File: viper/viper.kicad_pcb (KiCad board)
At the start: 2 copper layers, 49 parts, among them J1 Barrel_Jack, J10 DEBUG PINS, J11 Conn_01x05_Male, J12 Pimoroni BLINKT!, J13 Pimoroni BLINKT!, J2 Raspberry Pi Zero W2, J3 RPI Headers, J4 Adafruit CharliePlex Bonnet, J5 RPI Headers, J6 Pimoroni BLINKT!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

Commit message: feat: off switch routing
Signed-off-by: Matt Gleich <git@mattglei.ch>
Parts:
- J10, J7, J8: footprint Connector_PinHeader_2.54mm:PinHeader_2x20_P2.54mm_Vertical -> Connector_PinHeader_2.54mm:PinHeader_2x02_P2.54mm_Vertical
- R1, R10, R11, R12, R2, R3, R4, R5, R6, R7, R8, R9: value R_US -> 330Ω
- S1: value M2012SA1W03 -> MARK I
- S2: value M2012SA1W03 -> MARK II
- S3: value M2012SA1W03 -> MARK III
- S4: value M2012SA1W03 -> MARK IV
- S5: value M2012SA1W03 -> MASTER
- S6: value M2012SA1W03 -> MARK V
- moved D5 181.5 mm to (78.7, 21.3), turned to 180 degrees
- moved S3 179.3 mm to (77.9, 36.2), turned to 180 degrees
- moved D7 176.3 mm to (111.7, 21.5), turned to 180 degrees
- moved S4 167.2 mm to (110.7, 36.2), turned to 180 degrees
- moved D3 165.4 mm to (95.0, 21.4), turned to 180 degrees
- moved D2 160.3 mm to (62.0, 60.4), turned to 180 degrees
- moved R5 157.6 mm to (72.4, 29.0)
- moved D4 151.0 mm to (78.8, 60.4), turned to 180 degrees
- moved D13 146.6 mm to (125.8, 60.4)
- moved S2 144.6 mm to (94.1, 36.2), turned to 180 degrees
- moved D6 144.5 mm to (95.1, 60.4), turned to 180 degrees
- moved D10 139.5 mm to (128.3, 21.4), turned to 180 degrees
- moved S6 132.6 mm to (127.3, 36.2), turned to 180 degrees
- moved R7 131.9 mm to (105.4, 28.9)
- moved R10 127.0 mm to (122.0, 28.9)
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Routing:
- net GND: track 0.00 -> 142.3 mm
- net VBUS: track 68.6 -> 186.7 mm
- net Net-(R7-Pad2): track 0.00 -> 13.9 mm, vias 0 -> 2
- net Net-(R3-Pad2): track 0.00 -> 13.7 mm, vias 0 -> 2
- net Net-(R10-Pad2): track 0.00 -> 13.7 mm, vias 0 -> 2
- net Net-(R1-Pad2): track 0.00 -> 13.7 mm, vias 0 -> 2
- net Net-(R5-Pad2): track 0.00 -> 13.6 mm, vias 0 -> 2
- net Net-(R9-Pad2): track 0.00 -> 9.31 mm
- net Net-(D5-Pad2): track 0.00 -> 9.10 mm
- net Net-(D8-Pad2): track 0.00 -> 9.06 mm
- net Net-(D3-Pad2): track 0.00 -> 9.06 mm
- net Net-(D10-Pad2): track 0.00 -> 9.06 mm
- net Net-(D1-Pad2): track 0.00 -> 9.06 mm
- net Net-(D11-Pad1): track 0.00 -> 9.05 mm
- net Net-(D7-Pad2): track 0.00 -> 9.03 mm
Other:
- board outline added: 116.6 x 52.3 mm
- board text added: "MARK I"
- board text added: "MARK II"
- board text added: "MARK III"
- board text added: "MARK IV"
- board text added: "MARK V"
- board text added: "MASTER"

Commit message: feat: switch routing
Signed-off-by: Matt Gleich <git@mattglei.ch>
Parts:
- moved Brd1 169.0 mm to (216.7, 102.9)
- moved Brd2 169.0 mm to (245.2, 102.9)
- moved Brd3 169.0 mm to (325.2, 49.3)
- moved J10 169.0 mm to (296.6, 106.6)
- moved J13 169.0 mm to (289.1, 38.5)
- moved J4 169.0 mm to (277.0, 80.5)
- moved J5 169.0 mm to (277.0, 38.5)
- moved J6 169.0 mm to (184.9, 39.1)
- moved J7 169.0 mm to (361.4, 38.5)
- moved J8 169.0 mm to (304.1, 99.1)
- moved J9 169.0 mm to (283.0, 38.5)
- moved U1 169.0 mm to (262.9, 63.0)
- moved U2 169.0 mm to (214.7, 63.0)
- moved U3 169.0 mm to (238.8, 63.0)
- moved J11 169.0 mm to (313.4, 83.0)
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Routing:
- net VBUS: track 186.7 -> 234.4 mm
- net Net-(D13-Pad1): track 0.00 -> 9.08 mm
- net Net-(D4-Pad1): track 0.00 -> 9.05 mm
- net Net-(D2-Pad1): track 0.00 -> 9.05 mm
- net Net-(D6-Pad1): track 0.00 -> 9.05 mm
- net Net-(D9-Pad1): track 0.00 -> 9.03 mm

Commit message: feat: improve arrangement
Signed-off-by: Matt Gleich <git@mattglei.ch>
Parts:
- added J14: Adafruit Charlieplex Bonnet, Connector_PinHeader_2.54mm:PinHeader_2x20_P2.54mm_Vertical, F.Cu at (138.4, 152.5)
- J11: footprint Connector_PinHeader_2.54mm:PinHeader_2x20_P2.54mm_Vertical -> Connector_PinHeader_2.54mm:PinHeader_1x05_P2.54mm_Vertical
- J3: value RPI Headers -> Raspberry Pi Zero W2
- J5: value RPI Headers -> Adafruit CharliePlex Bonnet
- J9: value RPI Headers -> Pimoroni Inky pHAT
- moved J4 219.1 mm to (57.9, 78.4)
- moved U2 214.2 mm to (32.2, 175.1), turned to 180 degrees
- moved J12 212.0 mm to (92.9, 78.4)
- moved J13 189.3 mm to (104.0, 78.4)
- moved U3 175.5 mm to (106.7, 178.6), turned to 180 degrees
- moved Brd1 172.4 mm to (61.0, 177.0)
- moved J3 156.3 mm to (156.1, 78.4)
- moved U1 137.6 mm to (188.1, 178.4), turned to 180 degrees
- moved J11 132.4 mm to (215.9, 172.6)
- moved Brd2 108.3 mm to (136.9, 101.2)
- moved J5 93.7 mm to (192.2, 78.4)
- moved J6 80.2 mm to (115.0, 78.4)
- moved Brd3 75.5 mm to (400.3, 57.6)
- moved J10 75.5 mm to (371.6, 114.9)
- moved J7 75.5 mm to (436.5, 46.7)
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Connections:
- U3 pad 21: unconnected-(U3-Pad21) -> Net-(U3-Pad21)
- U3 pad 22: unconnected-(U3-Pad22) -> Net-(U3-Pad22)
- U3 pad 37: unconnected-(U3-Pad37) -> Net-(J14-Pad1)
- U3 pad 38: unconnected-(U3-Pad38) -> Net-(U3-Pad38)
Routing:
- net GND: track 142.3 -> 1033.6 mm, vias 0 -> 20
- net VBUS: track 234.4 -> 1051.6 mm, vias 0 -> 10
- net /SDA 02: track 0.00 -> 135.6 mm
- net /SCL 02: track 0.00 -> 129.2 mm
- net /GPIO 6: track 0.00 -> 112.1 mm
- net /GPIO 5: track 0.00 -> 110.4 mm
- net /GPIO 27: track 0.00 -> 87.9 mm
- net /GPIO 22: track 0.00 -> 87.7 mm
- net /GPIO 23: track 0.00 -> 72.1 mm
- net /GPIO 24: track 0.00 -> 72.1 mm
- net /SDA 01: track 0.00 -> 37.1 mm
- net /3.3V: track 0.00 -> 37.1 mm
- net /SCL 01: track 0.00 -> 37.1 mm
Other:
- board size 116.6 x 52.3 mm -> 269.5 x 197 mm

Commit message: feat: switches
Signed-off-by: Matt Gleich <git@mattglei.ch>
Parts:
- added D12: LED, LED_THT:LED_D5.0mm, F.Cu at (198.3, 46.2)
- added D14: LED, LED_THT:LED_D5.0mm, F.Cu at (200.9, 79.1)
- added J15: Adafruit Charlieplex Bonnet, Connector_PinHeader_2.54mm:PinHeader_2x20_P2.54mm_Vertical, F.Cu at (379.1, 87.1)
- added R13: 330Ω, Resistor_THT:R_Axial_DIN0309_L9.0mm_D3.2mm_P12.70mm_Horizontal, F.Cu at (193.2, 52.1)
- added R14: 330Ω, Resistor_THT:R_Axial_DIN0309_L9.0mm_D3.2mm_P12.70mm_Horizontal, F.Cu at (193.2, 73.1)
- added S7: M2012SA1W03, M2012SA1W03:M2012SA1W03, F.Cu at (401.6, 97.5)
- added S8: MARK VI, M2012SA1W03:M2012SA1W03, F.Cu at (199.7, 57.9)
- added U4: Pico, Pico:RPi_Pico_SMD_TH, F.Cu at (364.8, 111.3)
- J12, J6: value Pimoroni BLINKT! -> Pimoroni Inky pHAT
- J14: value Adafruit Charlieplex Bonnet -> DEBUG Pins; footprint Connector_PinHeader_2.54mm:PinHeader_2x20_P2.54mm_Vertical -> Connector_PinHeader_2.54mm:PinHeader_2x02_P2.54mm_Vertical
- J8: value DEBUG Pins -> DEBUG PINS
- J9: value Pimoroni Inky pHAT -> Pimoroni BLINKT!
- R1, R10, R11, R12, R2, R3, R4, R5, R6, R7, R8, R9: footprint Resistor_THT:R_Axial_DIN0207_L6.3mm_D2.5mm_P10.16mm_Horizontal -> Resistor_THT:R_Axial_DIN0309_L9.0mm_D3.2mm_P12.70mm_Horizontal
- moved J7 187.1 mm to (304.8, 179.7)
- moved J9 132.2 mm to (330.6, 176.0)
- moved J8 123.3 mm to (303.6, 204.7)
- moved J10 123.3 mm to (296.1, 212.3)
- moved J2 116.0 mm to (113.4, 149.6), turned to 180 degrees
- moved Brd3 109.7 mm to (310.7, 120.9)
- moved D10 67.7 mm to (182.6, 46.2)
- moved D5 67.6 mm to (132.8, 46.2)
- moved D3 67.5 mm to (149.0, 46.2)
- moved D7 67.3 mm to (165.6, 46.2)
- moved D8 67.3 mm to (98.5, 46.2)
- moved D1 67.1 mm to (115.6, 46.2)
- moved S6 66.7 mm to (181.6, 57.9)
- moved S3 66.5 mm to (131.9, 58.0)
- moved S2 66.4 mm to (148.0, 58.0)
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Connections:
- Brd2 pad 1: GND -> Net-(Brd2-Pad1)
- Brd2 pad 3: /SCL 02 -> Net-(Brd2-Pad3)
- Brd2 pad 4: /SDA 02 -> Net-(Brd2-Pad4)
- J12 pad 1: unconnected-(J12-Pad1) -> /3.3V
- J12 pad 11: unconnected-(J12-Pad11) -> /BUSY
- J12 pad 13: unconnected-(J12-Pad13) -> /RESET
- J12 pad 15: unconnected-(J12-Pad15) -> /DATA
- J12 pad 16: /GPIO 23 -> unconnected-(J12-Pad16)
- J12 pad 18: /GPIO 24 -> unconnected-(J12-Pad18)
- J12 pad 19: unconnected-(J12-Pad19) -> /SPI0 MOSI
- J12 pad 23: unconnected-(J12-Pad23) -> /SPI0 SCLK
- J12 pad 24: unconnected-(J12-Pad24) -> /CS
- J12 pad 3: unconnected-(J12-Pad3) -> /SDA 01
- J12 pad 4: VBUS -> unconnected-(J12-Pad4)
- J12 pad 5: unconnected-(J12-Pad5) -> /SCL 01
- J13 pad 16: /GPIO 27 -> /GPIO 23
- J13 pad 18: /GPIO 22 -> /GPIO 24
- J14 pad 2: VBUS -> Net-(J14-Pad2)
- J14 pad 3: Net-(U3-Pad22) -> Net-(J14-Pad3)
- J14 pad 4: unconnected-(J14-Pad4) -> Net-(J14-Pad4)
- J2 pad 11: unconnected-(J2-Pad11) -> /BUSY
- J2 pad 13: /GPIO 27 -> /RESET
- J2 pad 15: /GPIO 22 -> /DATA
- J2 pad 19: unconnected-(J2-Pad19) -> /SPI0 MOSI
- J2 pad 23: unconnected-(J2-Pad23) -> /SPI0 SCLK
- J2 pad 24: unconnected-(J2-Pad24) -> /CS
- J2 pad 27: /SDA 02 -> unconnected-(J2-Pad27)
- J2 pad 28: /SCL 02 -> unconnected-(J2-Pad28)
- J2 pad 29: /GPIO 5 -> /SCL 03
- J2 pad 31: /GPIO 6 -> unconnected-(J2-Pad31)
- J2 pad 7: unconnected-(J2-Pad7) -> /SDA 03
- J3 pad 11: unconnected-(J3-Pad11) -> /BUSY
- J3 pad 13: unconnected-(J3-Pad13) -> /RESET
- J3 pad 15: unconnected-(J3-Pad15) -> /DATA
- J3 pad 16: unconnected-(J3-Pad16) -> /GPIO 23
- J3 pad 18: unconnected-(J3-Pad18) -> /GPIO 24
- J3 pad 21: /SPI0 MISO -> unconnected-(J3-Pad21)
- J3 pad 24: /Chip Select -> /CS
- J3 pad 27: /SDA 02 -> unconnected-(J3-Pad27)
- J3 pad 28: /SCL 02 -> unconnected-(J3-Pad28)
- J3 pad 29: unconnected-(J3-Pad29) -> /SCL 03
- J3 pad 7: unconnected-(J3-Pad7) -> /SDA 03
- J4 pad 3: /SDA 01 -> /SDA 03
- J4 pad 5: /SCL 01 -> /SCL 03
- J5 pad 3: /SDA 01 -> /SDA 03
- J5 pad 5: /SCL 01 -> /SCL 03
- J6 pad 1: unconnected-(J6-Pad1) -> /3.3V
- J6 pad 11: unconnected-(J6-Pad11) -> /BUSY
- J6 pad 13: unconnected-(J6-Pad13) -> /RESET
- J6 pad 15: unconnected-(J6-Pad15) -> /DATA
- J6 pad 16: /GPIO 5 -> unconnected-(J6-Pad16)
- J6 pad 18: /GPIO 6 -> unconnected-(J6-Pad18)
- J6 pad 19: unconnected-(J6-Pad19) -> /SPI0 MOSI
- J6 pad 23: unconnected-(J6-Pad23) -> /SPI0 SCLK
- J6 pad 24: unconnected-(J6-Pad24) -> /CS
- J6 pad 3: unconnected-(J6-Pad3) -> /SDA 01
- J6 pad 4: VBUS -> unconnected-(J6-Pad4)
- J6 pad 5: unconnected-(J6-Pad5) -> /SCL 01
- J9 pad 16: unconnected-(J9-Pad16) -> /GPIO 23
- J9 pad 18: unconnected-(J9-Pad18) -> /GPIO 24
- J9 pad 2: unconnected-(J9-Pad2) -> VBUS
- U1 pad 20: unconnected-(U1-Pad20) -> Net-(U1-Pad20)
- U3 pad 21: Net-(U3-Pad21) -> Net-(Brd2-Pad3)
- U3 pad 22: Net-(U3-Pad22) -> Net-(Brd2-Pad4)
- U3 pad 37: Net-(J14-Pad1) -> unconnected-(U3-Pad37)
- U3 pad 38: Net-(U3-Pad38) -> Net-(Brd2-Pad1)
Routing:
- net VBUS: track 1051.6 -> 136.8 mm, vias 10 -> 2
- net GND: track 1033.6 -> 289.2 mm, vias 20 -> 6
- net /SDA 02: track 135.6 -> 0.00 mm
- net /SCL 02: track 129.2 -> 0.00 mm
- net /GPIO 6: track 112.1 -> 0.00 mm
- net /GPIO 5: track 110.4 -> 0.00 mm
- net /GPIO 27: track 87.9 -> 0.00 mm
- net /GPIO 22: track 87.7 -> 0.00 mm
- net /GPIO 23: track 72.1 -> 0.00 mm
- net /GPIO 24: track 72.1 -> 0.00 mm
- net /SDA 03: track 0.00 -> 69.4 mm
- net /SCL 03: track 0.00 -> 68.3 mm
- net /SDA 01: track 37.1 -> 0.00 mm
- net /SCL 01: track 37.1 -> 0.00 mm
- net /3.3V: track 37.1 -> 71.0 mm
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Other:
- board text added: "MARK VI"
- board text added: "OFF"
- board text added: "ON"

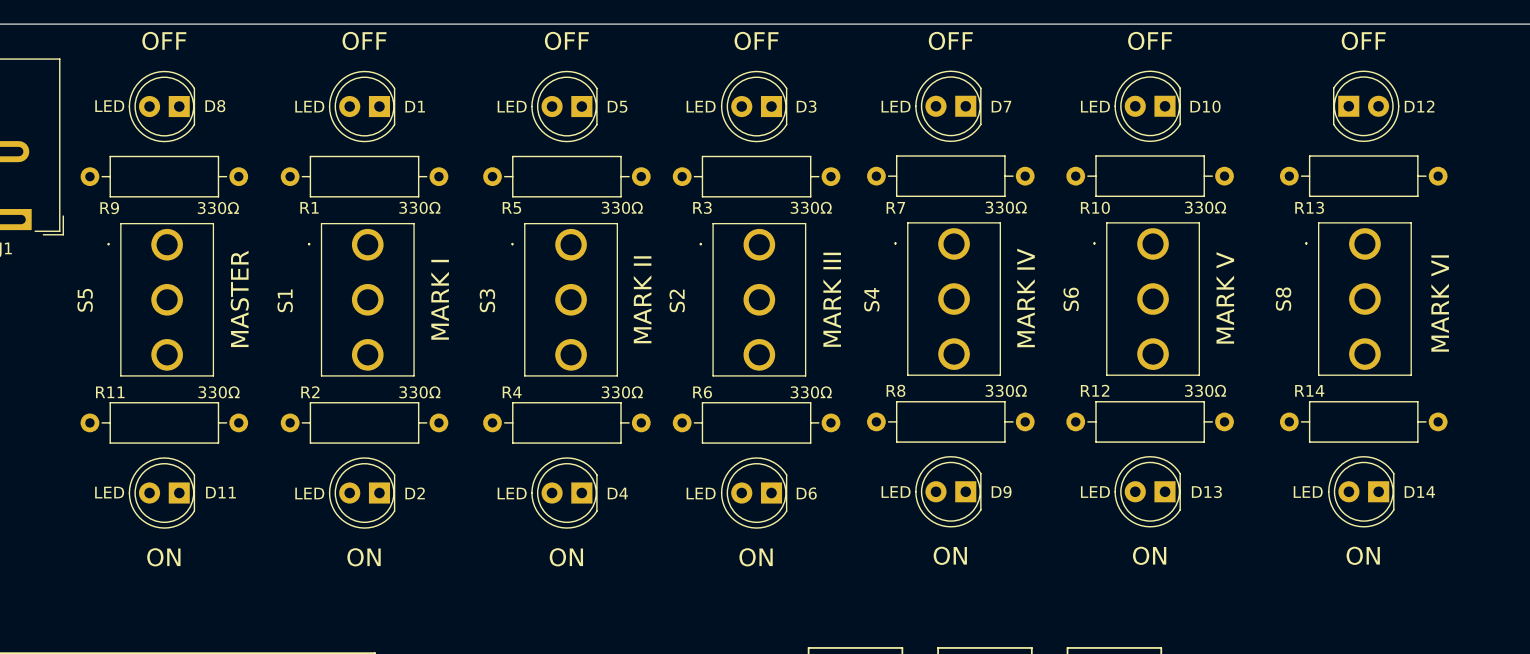
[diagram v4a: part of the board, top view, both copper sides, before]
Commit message: feat: align switches
Signed-off-by: Matt Gleich <git@mattglei.ch>
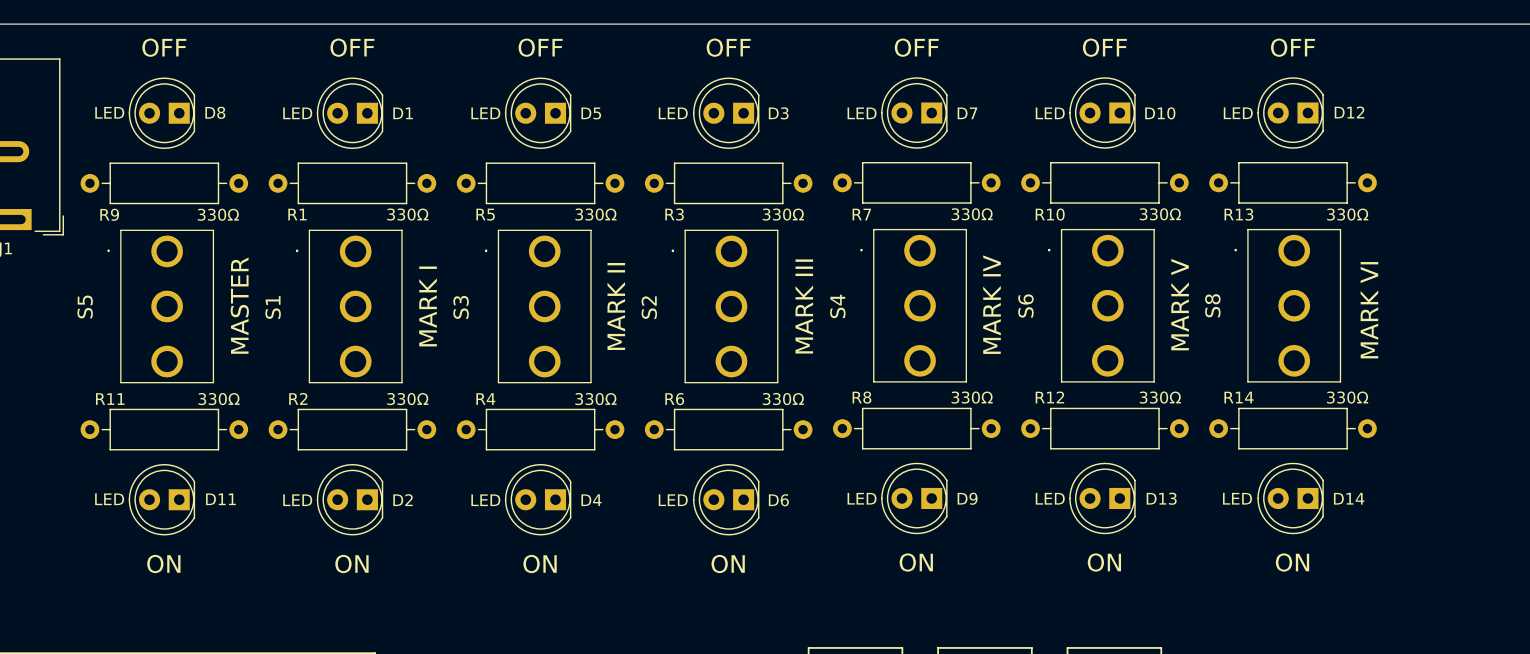
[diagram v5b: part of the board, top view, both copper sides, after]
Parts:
- moved R13 6.06 mm to (187.2, 52.7)
- moved R14 6.06 mm to (187.2, 73.7)
- moved D14 6.06 mm to (194.8, 79.6)
- moved S8 6.06 mm to (193.6, 58.5)
- moved R10 3.90 mm to (171.1, 52.7)
- moved R12 3.90 mm to (171.1, 73.7)
- moved S6 3.90 mm to (177.7, 58.5)
- moved D10 3.90 mm to (178.8, 46.7)
- moved D13 3.90 mm to (178.8, 79.6)
- moved D12 3.53 mm to (194.8, 46.7), turned to 180 degrees
- moved R7 2.96 mm to (155.1, 52.7)
- moved R8 2.96 mm to (155.1, 73.7)
- moved S4 2.96 mm to (161.7, 58.5)
- moved D7 2.96 mm to (162.7, 46.7)
- moved D9 2.96 mm to (162.7, 79.6)
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
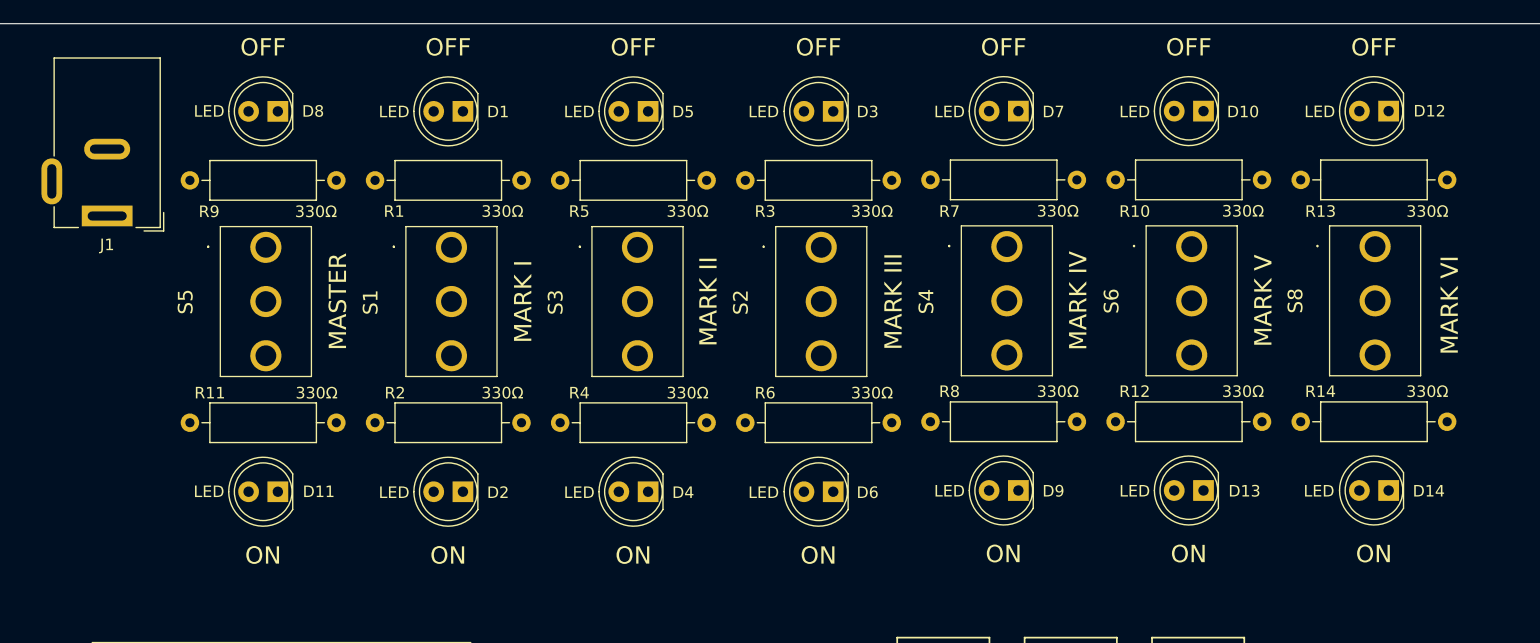
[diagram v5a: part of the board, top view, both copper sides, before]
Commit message: feat: route switches
Signed-off-by: Matt Gleich <git@mattglei.ch>
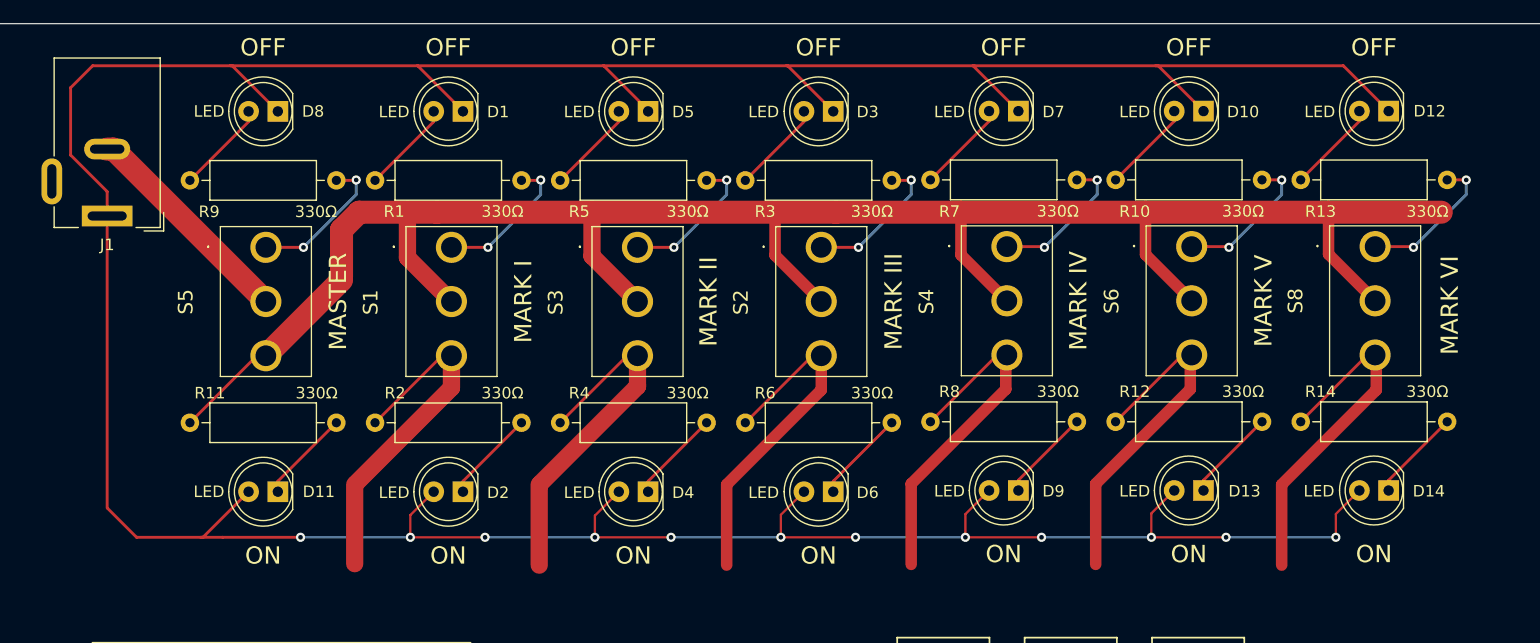
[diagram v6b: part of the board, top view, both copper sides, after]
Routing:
- net VBUS: track 136.8 -> 514.2 mm
- net GND: track 289.2 -> 620.2 mm, vias 6 -> 18
- net Net-(R13-Pad2): track 0.00 -> 13.2 mm, vias 0 -> 2
- net Net-(R7-Pad2): track 0.00 -> 13.1 mm, vias 0 -> 2
- net Net-(R10-Pad2): track 0.00 -> 13.0 mm, vias 0 -> 2
- net Net-(R3-Pad2): track 0.00 -> 13.0 mm, vias 0 -> 2
- net Net-(R1-Pad2): track 0.00 -> 12.8 mm, vias 0 -> 2
- net Net-(R5-Pad2): track 0.00 -> 12.8 mm, vias 0 -> 2
- net Net-(R9-Pad2): track 0.30 -> 13.0 mm, vias 0 -> 2
- net Net-(D8-Pad2): track 0.00 -> 8.09 mm
- net Net-(D5-Pad2): track 0.00 -> 8.09 mm
- net Net-(D1-Pad2): track 0.00 -> 8.09 mm
- net Net-(D3-Pad2): track 0.00 -> 8.09 mm
- net Net-(D4-Pad1): track 0.00 -> 8.09 mm
- net Net-(D2-Pad1): track 0.00 -> 8.09 mm
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
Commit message: feat: mark i
Signed-off-by: Matt Gleich <git@mattglei.ch>
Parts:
- moved Brd3 96.4 mm to (394.2, 72.7)
- moved Brd2 96.4 mm to (282.4, 75.9)
- moved J3 96.4 mm to (301.6, 53.0)
- moved J5 96.4 mm to (337.8, 53.0)
- moved J6 96.4 mm to (260.6, 53.1)
- moved J13 17.8 mm to (183.8, 102.7)
- moved J2 4.86 mm to (108.6, 150.0)
- moved J12 4.27 mm to (150.9, 102.7)
- moved J4 2.16 mm to (118.1, 102.5)
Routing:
- net VBUS: track 514.2 -> 761.5 mm, vias 2 -> 1
- net /GPIO 24: track 0.00 -> 142.0 mm
- net /GPIO 23: track 0.00 -> 132.6 mm
- net GND: track 620.2 -> 748.1 mm, vias 18 -> 19
- net /CS: track 0.00 -> 113.9 mm, vias 0 -> 1
- net /SPI0 SCLK: track 0.00 -> 99.6 mm, vias 0 -> 1
- net /SPI0 MOSI: track 0.00 -> 98.8 mm, vias 0 -> 1
- net /DATA: track 0.00 -> 94.9 mm, vias 0 -> 1
- net /RESET: track 0.00 -> 93.9 mm, vias 0 -> 1
- net /BUSY: track 0.00 -> 92.9 mm, vias 0 -> 1
- net /SCL 01: track 0.00 -> 90.6 mm, vias 0 -> 1
- net /SDA 01: track 0.00 -> 89.6 mm, vias 0 -> 1
- net /SCL 03: track 68.3 -> 45.3 mm, vias 0 -> 1
- net /3.3V: track 71.0 -> 91.6 mm
- net /SDA 03: track 69.4 -> 56.8 mm, vias 0 -> 1
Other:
- board size 269.5 x 197 mm -> 258.2 x 197 mm
